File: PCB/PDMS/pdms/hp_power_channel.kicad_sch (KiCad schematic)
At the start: 0 parts

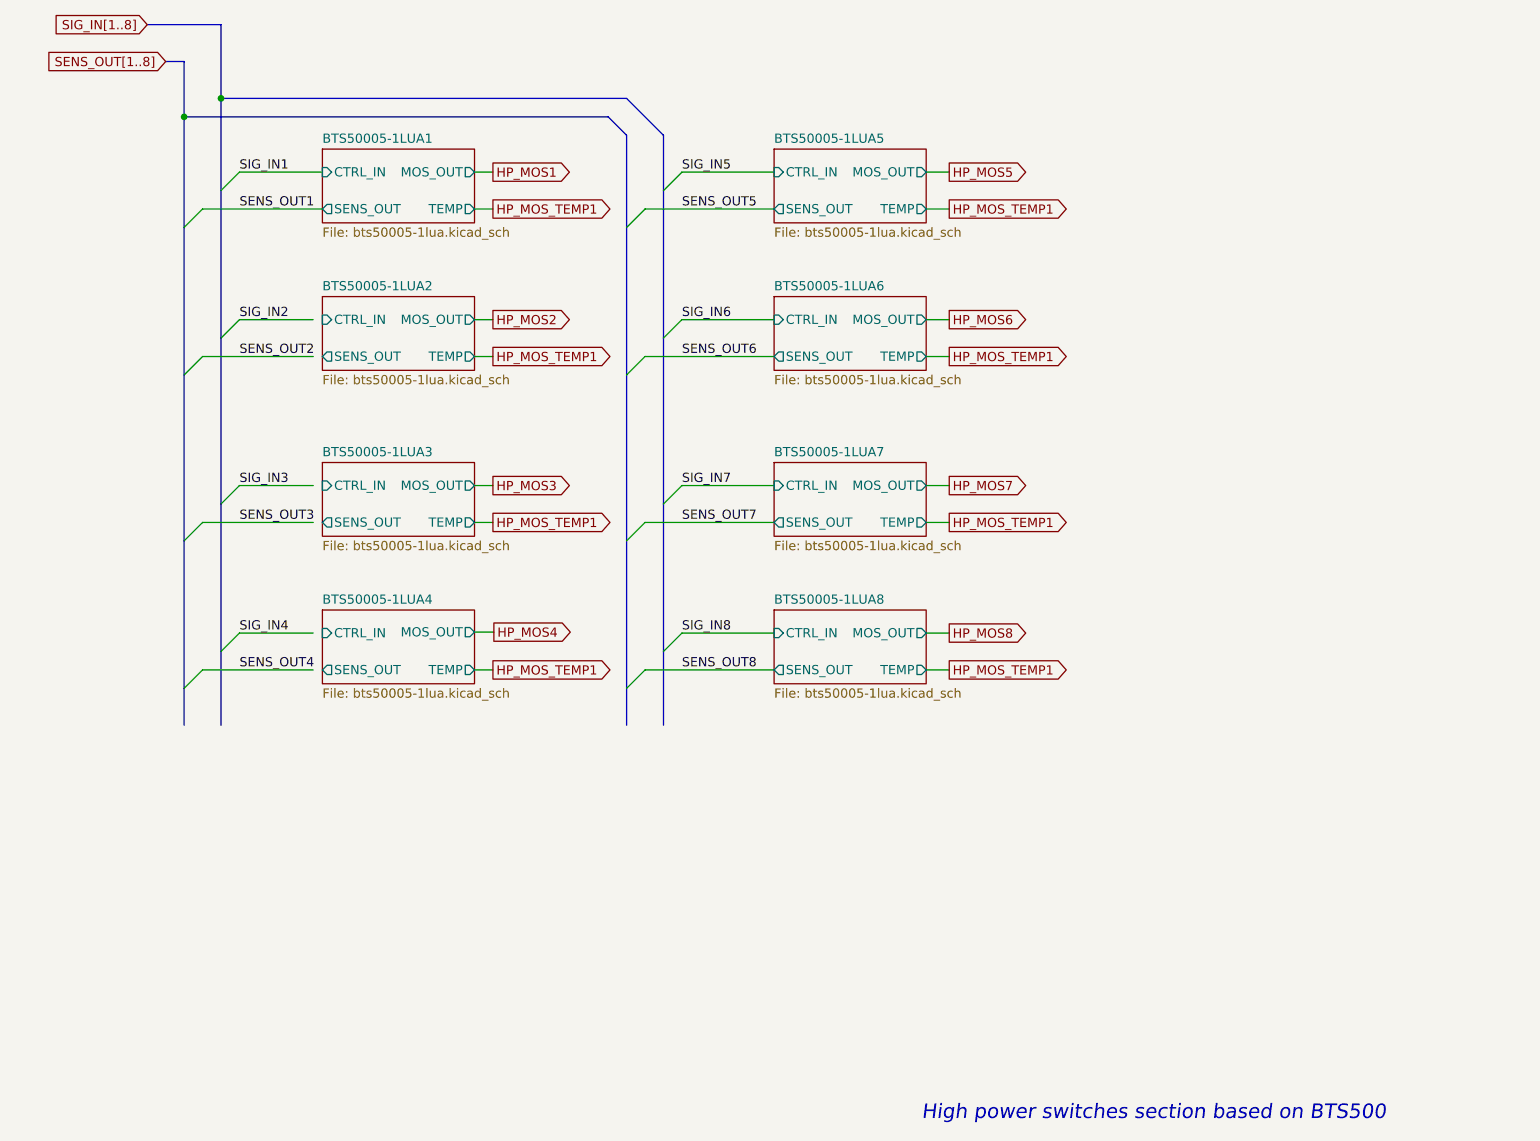
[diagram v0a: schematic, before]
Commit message: Finished layout - w/o stiching
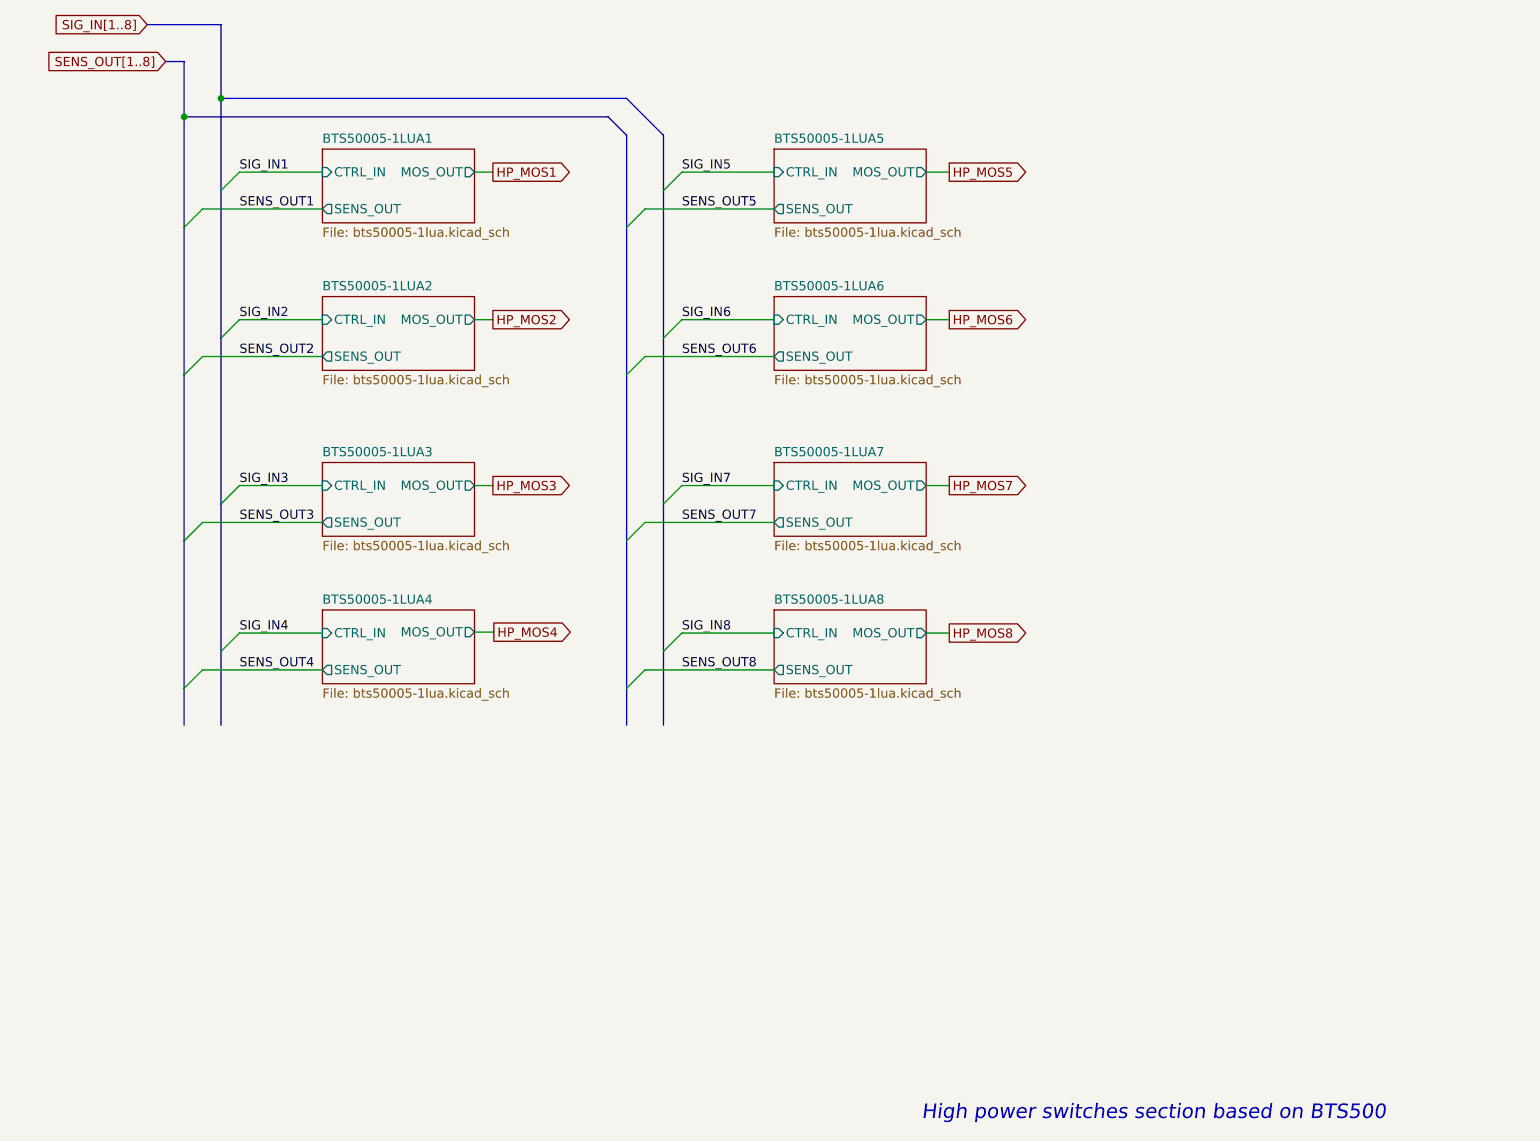
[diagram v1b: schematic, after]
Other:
- sheet BTS50005-1LUA1 ports: added none; removed TEMP
- sheet BTS50005-1LUA2 ports: added none; removed TEMP
- sheet BTS50005-1LUA3 ports: added none; removed TEMP
- sheet BTS50005-1LUA4 ports: added none; removed TEMP
- sheet BTS50005-1LUA5 ports: added none; removed TEMP
- sheet BTS50005-1LUA6 ports: added none; removed TEMP
- sheet BTS50005-1LUA7 ports: added none; removed TEMP
- sheet BTS50005-1LUA8 ports: added none; removed TEMP
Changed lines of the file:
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@@
     (stroke (width 0) (type default) (color 0 0 0 0))
   )
-  (wire (pts (xy 125.095 85.725) (xy 127.635 85.725))
-    (stroke (width 0) (type default) (color 0 0 0 0))
-  )
-  (wire (pts (xy 187.325 85.725) (xy 190.5 85.725))
+  (wire (pts (xy 87.63 128.905) (xy 104.14 128.905))
     (stroke (width 0) (type default) (color 0 0 0 0))
   )
@@
     (stroke (width 0) (type default) (color 0 0 0 0))
   )
-  (wire (pts (xy 87.63 108.585) (xy 102.87 108.585))
+  (wire (pts (xy 87.63 108.585) (xy 104.14 108.585))
     (stroke (width 0) (type default) (color 0 0 0 0))
   )
@@
     (stroke (width 0) (type default) (color 0 0 0 0))
   )
-  (wire (pts (xy 187.325 108.585) (xy 190.5 108.585))
-    (stroke (width 0) (type default) (color 0 0 0 0))
-  )
-  (wire (pts (xy 87.63 85.725) (xy 102.87 85.725))
+  (wire (pts (xy 87.63 85.725) (xy 104.14 85.725))
     (stroke (width 0) (type default) (color 0 0 0 0))
   )
@@
     (stroke (width 0) (type default) (color 0 0 0 0))
   )
-  (wire (pts (xy 187.325 65.405) (xy 190.5 65.405))
-    (stroke (width 0) (type default) (color 0 0 0 0))
-  )
   (wire (pts (xy 153.67 103.505) (xy 166.37 103.505))
     (stroke (width 0) (type default) (color 0 0 0 0))
@@
     (stroke (width 0) (type default) (color 0 0 0 0))
   )
+  (wire (pts (xy 92.71 123.825) (xy 104.14 123.825))
+    (stroke (width 0) (type default) (color 0 0 0 0))
+  )
   (bus (pts (xy 82.55 45.085) (xy 85.09 45.085))
     (stroke (width 0) (type default) (color 0 0 0 0))
   )
-  (wire (pts (xy 92.71 103.505) (xy 102.87 103.505))
+  (wire (pts (xy 92.71 103.505) (xy 104.14 103.505))
     (stroke (width 0) (type default) (color 0 0 0 0))
   )
@@
     (stroke (width 0) (type default) (color 0 0 0 0))
   )
-  (wire (pts (xy 125.095 128.905) (xy 127.635 128.905))
-    (stroke (width 0) (type default) (color 0 0 0 0))
-  )
   (bus (pts (xy 151.13 83.185) (xy 151.13 106.045))
     (stroke (width 0) (type default) (color 0 0 0 0))
@@
     (stroke (width 0) (type default) (color 0 0 0 0))
   )
-  (wire (pts (xy 125.095 108.585) (xy 127.635 108.585))
-    (stroke (width 0) (type default) (color 0 0 0 0))
-  )
   (wire (pts (xy 153.67 80.645) (xy 166.37 80.645))
     (stroke (width 0) (type default) (color 0 0 0 0))
@@
     (stroke (width 0) (type default) (color 0 0 0 0))
   )
-  (wire (pts (xy 92.71 80.645) (xy 102.87 80.645))
-    (stroke (width 0) (type default) (color 0 0 0 0))
-  )
-  (wire (pts (xy 87.63 128.905) (xy 102.87 128.905))
+  (wire (pts (xy 92.71 80.645) (xy 104.14 80.645))
     (stroke (width 0) (type default) (color 0 0 0 0))
   )
@@
     (stroke (width 0) (type default) (color 0 0 0 0))
   )
-  (wire (pts (xy 125.095 65.405) (xy 127.635 65.405))
-    (stroke (width 0) (type default) (color 0 0 0 0))
-  )
-  (wire (pts (xy 187.325 128.905) (xy 190.5 128.905))
-    (stroke (width 0) (type default) (color 0 0 0 0))
-  )
   (wire (pts (xy 125.095 123.698) (xy 127.762 123.698))
     (stroke (width 0) (type default) (color 0 0 0 0))
@@
   )
   (bus (pts (xy 146.05 67.945) (xy 146.05 88.265))
-    (stroke (width 0) (type default) (color 0 0 0 0))
-  )
-  (wire (pts (xy 92.71 123.825) (xy 102.87 123.825))
     (stroke (width 0) (type default) (color 0 0 0 0))
   )
@@
   (label "SENS_OUT4" (at 92.71 128.905 0)
     (effects (font (size 1.27 1.27)) (justify left bottom))
-  )
-  (global_label "HP_MOS_TEMP1" (shape output) (at 127.635 108.585 0) (fields_autoplaced)
-    (effects (font (size 1.27 1.27)) (justify left))
-    (property "Intersheet References" "${INTERSHEET_REFS}" (id 0) (at 144.6229 108.5056 0)
-      (effects (font (size 1.27 1.27)) (justify left) hide)
-    )
   )
   (global_label "HP_MOS5" (shape output) (at 190.5 60.325 0) (fields_autoplaced)
@@
     )
   )
-  (global_label "HP_MOS_TEMP1" (shape output) (at 127.635 128.905 0) (fields_autoplaced)
-    (effects (font (size 1.27 1.27)) (justify left))
-    (property "Intersheet References" "${INTERSHEET_REFS}" (id 0) (at 144.6229 128.8256 0)
-      (effects (font (size 1.27 1.27)) (justify left) hide)
-    )
-  )
   (global_label "SIG_IN[1..8]" (shape input) (at 80.01 40.005 180) (fields_autoplaced)
     (effects (font (size 1.27 1.27)) (justify right))
@@
     )
   )
-  (global_label "HP_MOS_TEMP1" (shape output) (at 127.635 65.405 0) (fields_autoplaced)
-    (effects (font (size 1.27 1.27)) (justify left))
-    (property "Intersheet References" "${INTERSHEET_REFS}" (id 0) (at 144.6229 65.3256 0)
-      (effects (font (size 1.27 1.27)) (justify left) hide)
-    )
-  )
-  (global_label "HP_MOS_TEMP1" (shape output) (at 190.5 65.405 0) (fields_autoplaced)
-    (effects (font (size 1.27 1.27)) (justify left))
-    (property "Intersheet References" "${INTERSHEET_REFS}" (id 0) (at 207.4879 65.3256 0)
-      (effects (font (size 1.27 1.27)) (justify left) hide)
-    )
-  )
   (global_label "HP_MOS1" (shape output) (at 127.635 60.325 0) (fields_autoplaced)
     (effects (font (size 1.27 1.27)) (justify left))
@@
     )
   )
-  (global_label "HP_MOS_TEMP1" (shape output) (at 190.5 128.905 0) (fields_autoplaced)
-    (effects (font (size 1.27 1.27)) (justify left))
-    (property "Intersheet References" "${INTERSHEET_REFS}" (id 0) (at 207.4879 128.8256 0)
-      (effects (font (size 1.27 1.27)) (justify left) hide)
-    )
-  )
-  (global_label "HP_MOS_TEMP1" (shape output) (at 190.5 85.725 0) (fields_autoplaced)
-    (effects (font (size 1.27 1.27)) (justify left))
-    (property "Intersheet References" "${INTERSHEET_REFS}" (id 0) (at 207.4879 85.6456 0)
-      (effects (font (size 1.27 1.27)) (justify left) hide)
-    )
-  )
-  (global_label "HP_MOS_TEMP1" (shape output) (at 190.5 108.585 0) (fields_autoplaced)
-    (effects (font (size 1.27 1.27)) (justify left))
-    (property "Intersheet References" "${INTERSHEET_REFS}" (id 0) (at 207.4879 108.5056 0)
-      (effects (font (size 1.27 1.27)) (justify left) hide)
-    )
-  )
-  (global_label "HP_MOS_TEMP1" (shape output) (at 127.635 85.725 0) (fields_autoplaced)
-    (effects (font (size 1.27 1.27)) (justify left))
-    (property "Intersheet References" "${INTERSHEET_REFS}" (id 0) (at 144.6229 85.6456 0)
-      (effects (font (size 1.27 1.27)) (justify left) hide)
-    )
-  )
   (sheet (at 166.37 57.15) (size 20.955 10.16) (fields_autoplaced)
     (stroke (width 0.1524) (type solid) (color 0 0 0 0))
@@
       (effects (font (size 1.27 1.27)) (justify left))
     )
-    (pin "TEMP" output (at 187.325 65.405 0)
-      (effects (font (size 1.27 1.27)) (justify right))
-    )
   )
   (sheet (at 166.37 120.65) (size 20.955 10.16) (fields_autoplaced)
@@
       (effects (font (size 1.27 1.27)) (justify left))
     )
-    (pin "TEMP" output (at 187.325 128.905 0)
-      (effects (font (size 1.27 1.27)) (justify right))
-    )
   )
   (sheet (at 104.14 100.33) (size 20.955 10.16) (fields_autoplaced)
@@
       (effects (font (size 1.27 1.27)) (justify left))
     )
-    (pin "TEMP" output (at 125.095 108.585 0)
-      (effects (font (size 1.27 1.27)) (justify right))
-    )
   )
   (sheet (at 104.14 120.65) (size 20.955 10.16) (fields_autoplaced)
@@
       (effects (font (size 1.27 1.27)) (justify left))
     )
-    (pin "TEMP" output (at 125.095 128.905 0)
-      (effects (font (size 1.27 1.27)) (justify right))
-    )
   )
   (sheet (at 166.37 100.33) (size 20.955 10.16) (fields_autoplaced)
@@
       (effects (font (size 1.27 1.27)) (justify left))
     )
-    (pin "TEMP" output (at 187.325 108.585 0)
-      (effects (font (size 1.27 1.27)) (justify right))
-    )
   )
   (sheet (at 104.14 77.47) (size 20.955 10.16) (fields_autoplaced)
@@
       (effects (font (size 1.27 1.27)) (justify left))
     )
-    (pin "TEMP" output (at 125.095 85.725 0)
-      (effects (font (size 1.27 1.27)) (justify right))
-    )
     (pin "MOS_OUT" output (at 125.095 80.645 0)
       (effects (font (size 1.27 1.27)) (justify right))
@@
       (effects (font (size 1.27 1.27)) (justify left))
     )
-    (pin "TEMP" output (at 125.095 65.405 0)
-      (effects (font (size 1.27 1.27)) (justify right))
-    )
     (pin "MOS_OUT" output (at 125.095 60.325 0)
       (effects (font (size 1.27 1.27)) (justify right))
@@
       (effects (font (size 1.27 1.27)) (justify left))
     )
-    (pin "TEMP" output (at 187.325 85.725 0)
-      (effects (font (size 1.27 1.27)) (justify right))
-    )
-  )
+  )

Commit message: Clean-up of schematics
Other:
- note added: "High current - power channels - BTS500"
- note removed: "High power switches section based on BTS500"
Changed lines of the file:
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@@
     (stroke (width 0) (type default) (color 0 0 0 0))
   )
-  (text "High power switches section based on BTS500" (at 186.69 191.135 0)
+  (text "High current - power channels - BTS500" (at 186.69 191.135 0)
     (effects (font (size 2 2) italic) (justify left bottom))
   )

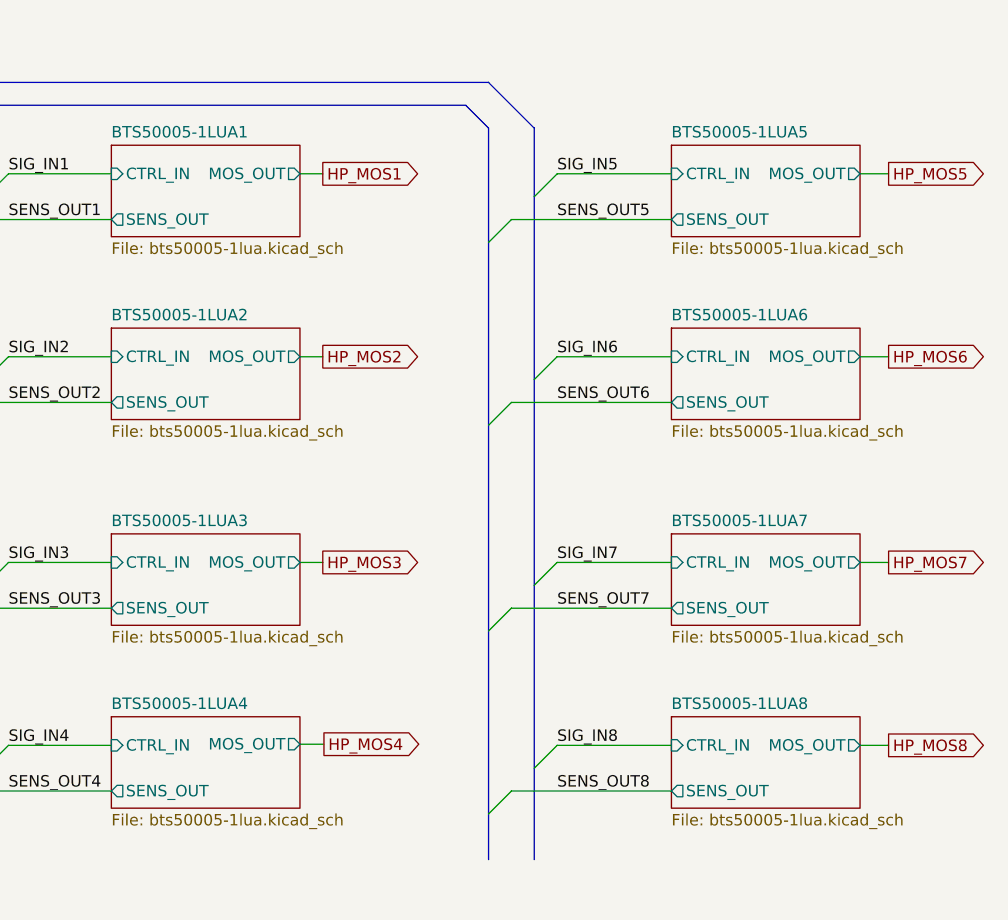
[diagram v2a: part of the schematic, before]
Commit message: Added fuses to main output channels
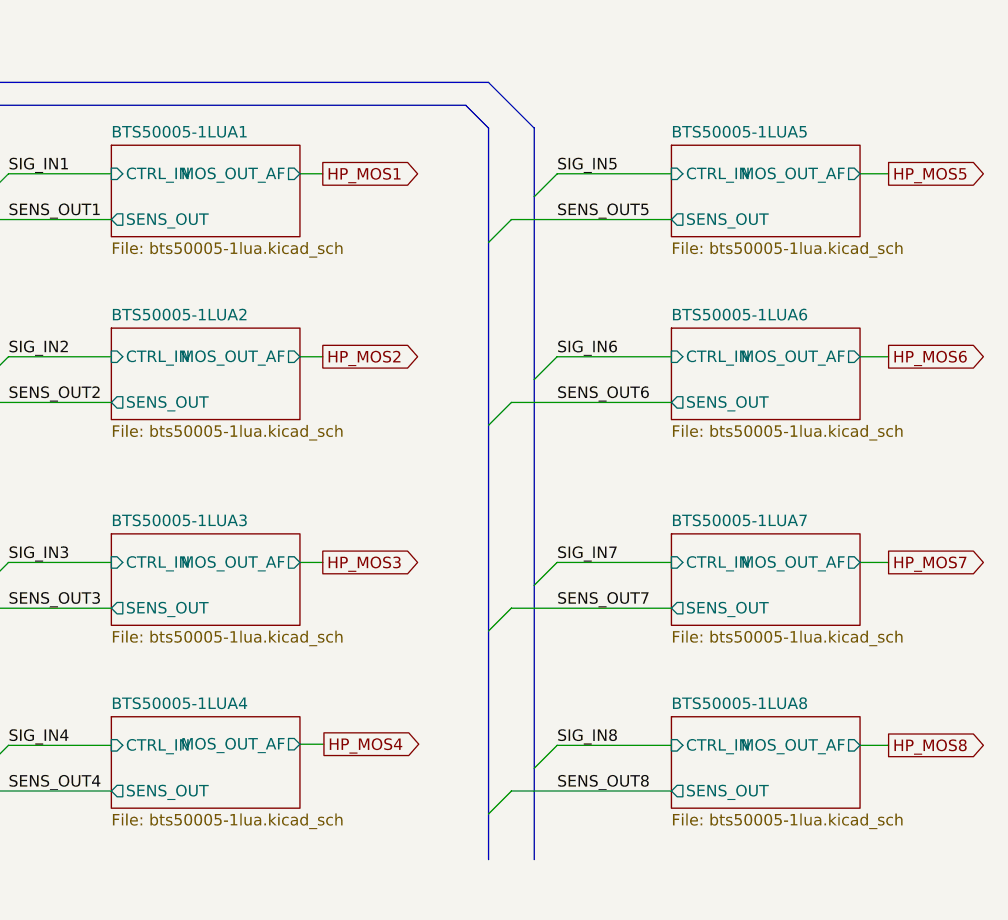
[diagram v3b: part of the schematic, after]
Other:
- sheet BTS50005-1LUA1 ports: added MOS_OUT_AF; removed MOS_OUT
- sheet BTS50005-1LUA2 ports: added MOS_OUT_AF; removed MOS_OUT
- sheet BTS50005-1LUA3 ports: added MOS_OUT_AF; removed MOS_OUT
- sheet BTS50005-1LUA4 ports: added MOS_OUT_AF; removed MOS_OUT
- sheet BTS50005-1LUA5 ports: added MOS_OUT_AF; removed MOS_OUT
- sheet BTS50005-1LUA6 ports: added MOS_OUT_AF; removed MOS_OUT
- sheet BTS50005-1LUA7 ports: added MOS_OUT_AF; removed MOS_OUT
- sheet BTS50005-1LUA8 ports: added MOS_OUT_AF; removed MOS_OUT
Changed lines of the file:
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@@
       (effects (font (size 1.27 1.27)) (justify left))
     )
-    (pin "MOS_OUT" output (at 187.325 60.325 0)
+    (pin "MOS_OUT_AF" output (at 187.325 60.325 0)
       (effects (font (size 1.27 1.27)) (justify right))
     )
@@
       (effects (font (size 1.27 1.27)) (justify left))
     )
-    (pin "MOS_OUT" output (at 187.325 123.825 0)
+    (pin "MOS_OUT_AF" output (at 187.325 123.825 0)
       (effects (font (size 1.27 1.27)) (justify right))
     )
@@
       (effects (font (size 1.27 1.27)) (justify left))
     )
-    (pin "MOS_OUT" output (at 125.095 103.505 0)
+    (pin "MOS_OUT_AF" output (at 125.095 103.505 0)
       (effects (font (size 1.27 1.27)) (justify right))
     )
@@
       (effects (font (size 1.27 1.27)) (justify left))
     )
-    (pin "MOS_OUT" output (at 125.095 123.698 0)
+    (pin "MOS_OUT_AF" output (at 125.095 123.698 0)
       (effects (font (size 1.27 1.27)) (justify right))
     )
@@
       (effects (font (size 1.27 1.27)) (justify left))
     )
-    (pin "MOS_OUT" output (at 187.325 103.505 0)
+    (pin "MOS_OUT_AF" output (at 187.325 103.505 0)
       (effects (font (size 1.27 1.27)) (justify right))
     )
@@
       (effects (font (size 1.27 1.27)) (justify left))
     )
-    (pin "MOS_OUT" output (at 125.095 80.645 0)
+    (pin "MOS_OUT_AF" output (at 125.095 80.645 0)
       (effects (font (size 1.27 1.27)) (justify right))
     )
@@
       (effects (font (size 1.27 1.27)) (justify left))
     )
-    (pin "MOS_OUT" output (at 125.095 60.325 0)
+    (pin "MOS_OUT_AF" output (at 125.095 60.325 0)
       (effects (font (size 1.27 1.27)) (justify right))
     )
@@
       (effects (font (size 1.27 1.27)) (justify left))
     )
-    (pin "MOS_OUT" output (at 187.325 80.645 0)
+    (pin "MOS_OUT_AF" output (at 187.325 80.645 0)
       (effects (font (size 1.27 1.27)) (justify right))
     )
